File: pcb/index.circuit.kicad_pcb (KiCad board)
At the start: 2 copper layers, 102.2 x 63.8 mm, 36 parts, among them Q1 AO3401A, U1 ESP32_S3_WROOM_1_N16R8, U2 MAX98357AETE_T

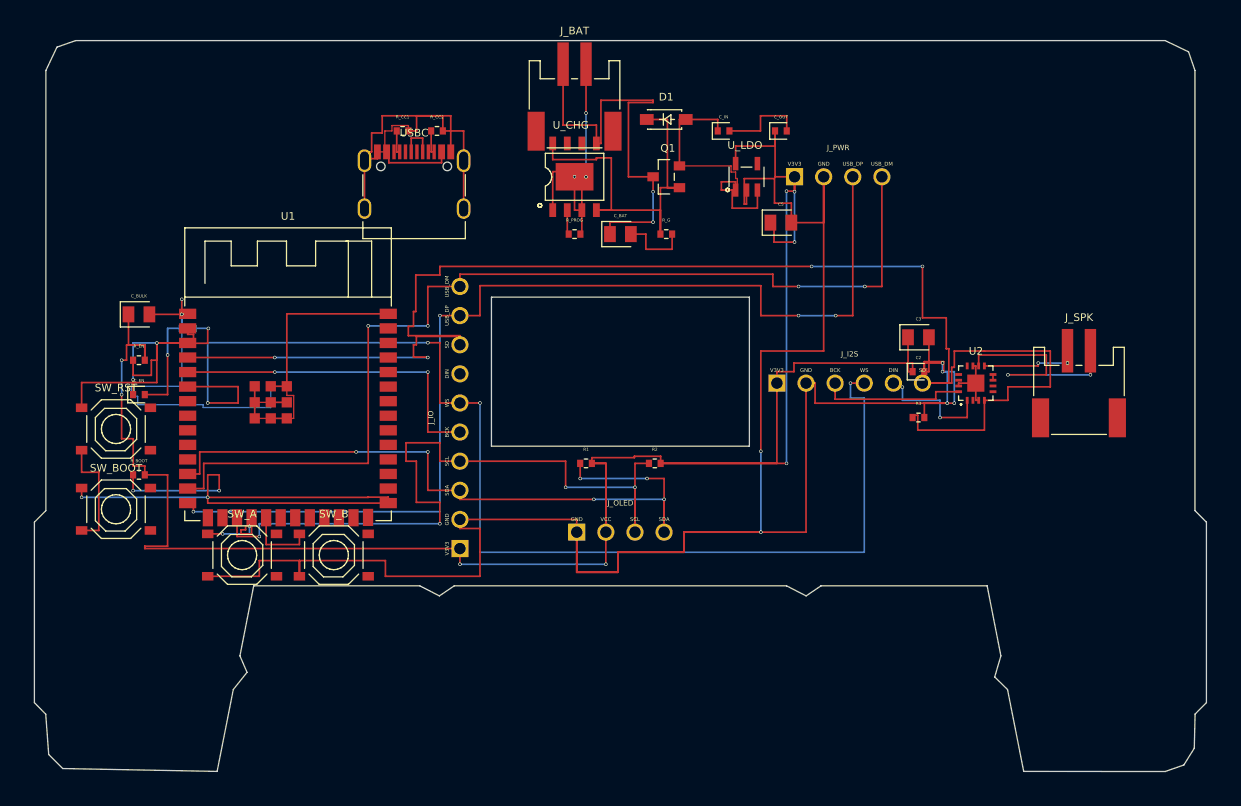
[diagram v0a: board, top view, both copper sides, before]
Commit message: pcb: fabbable cassette floorplan + headless IPC routing pipeline
Re-floorplan respecting ALL cassette cutouts (OLED window / 2 reel holes /
4 screw holes / bottom head-notch): spread the blocks across the board,
narrow the ESP32 column to fit beside the reel, and drop the now-redundant
breakout headers (J_IO/J_I2S/J_PWR) + reset/boot buttons (native-USB esptool
programming). All three placement gates pass: every part inside the outline,
0 courtyard overlaps, ~1 unrouted with the holes kept out. Routed via the IPC
pipeline (Freerouting -> kipy inject) with a GND pour; net fragments reconciled.

New place->route tooling (also in the global pcb-layout skill):
  route.sh, merge_nets.py, add_cutout_keepouts.py, drc_check.py,
  add_plane.py, apply_ses_ipc.py. Interior holes recovered from the CAD
  source of truth into lib/cassette_holes.json.

Co-Authored-By: Claude Opus 4.8 (1M context) <noreply@anthropic.com>
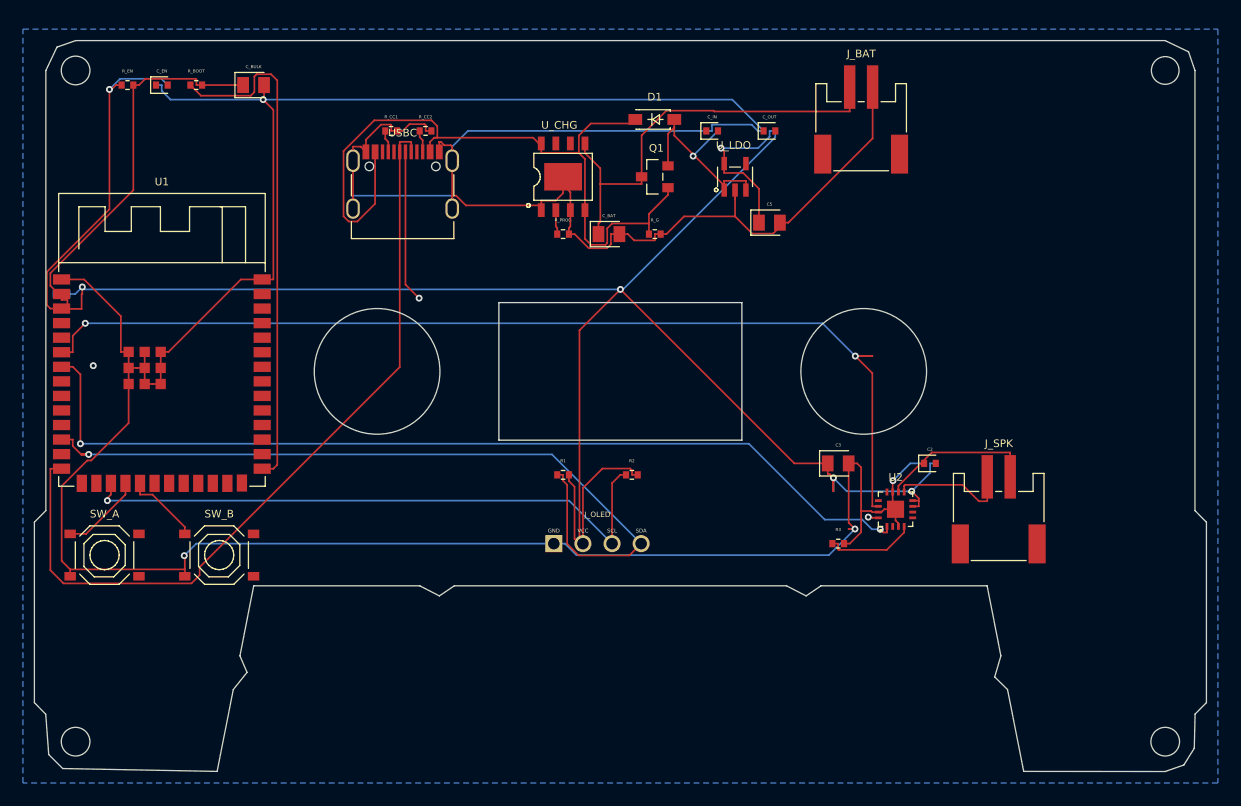
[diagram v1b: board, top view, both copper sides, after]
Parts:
- removed J_I2S: J_I2S, tscircuit:pin_header_pinrow6
- removed J_IO: J_IO, tscircuit:pin_header_pinrow10
- removed J_PWR: J_PWR, tscircuit:pin_header_pinrow4
- removed SW_BOOT, SW_RST: TS_1187A_B_A_B, tscircuit:TS_1187A_B_A_B
- moved R_BOOT 34.4 mm to (63.0, 72.0)
- moved C_EN 27.1 mm to (60.0, 72.0)
- moved J_BAT 25.1 mm to (121.0, 75.0)
- moved R_EN 24.0 mm to (57.0, 72.0)
- moved C_BULK 22.4 mm to (68.0, 72.0)
- moved C3 13.0 mm to (119.0, 105.0)
- moved J_SPK 13.0 mm to (133.0, 109.0)
- moved R3 13.0 mm to (119.0, 112.0)
- moved U2 13.0 mm to (124.0, 109.0)
- moved SW_A 12.0 mm to (55.0, 113.0)
- moved C1 11.4 mm to (51.2, 90.2)
- moved U1 11.4 mm to (60.0, 98.0)
- moved SW_B 10.0 mm to (65.0, 113.0)
- moved C2 8.06 mm to (127.0, 105.0)
- moved J_OLED 2.24 mm to (98.0, 112.0)
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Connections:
- J_OLED pad 3: .mcu .J_IO .SCL to .display .J_OLED .SCL -> SCL
- J_OLED pad 4: .mcu .J_IO .SDA to .display .J_OLED .SDA -> SDA
- R1 pad 2: J_OLED.VCC to net.V3V3 -> V3V3
- R2 pad 2: J_OLED.VCC to net.V3V3 -> V3V3
- R3 pad 1: J_I2S.SD to U2.SD_MODE -> SD
- U1 pad 12: U1.IO8 to J_IO.SDA -> SDA
- U1 pad 13: U1.IO19 to J_IO.USB_DM -> USB_DM
- U1 pad 14: U1.IO20 to J_IO.USB_DP -> USB_DP
- U1 pad 17: U1.IO9 to J_IO.SCL -> SCL
- U1 pad 4: U1.IO4 to J_IO.SD -> SD
- U1 pad 5: U1.IO5 to J_IO.BCK -> BCK
- U1 pad 6: U1.IO6 to J_IO.WS -> WS
- U1 pad 7: U1.IO7 to J_IO.DIN -> DIN
- U2 pad 1: J_I2S.DIN to U2.DIN -> DIN
- U2 pad 14: J_I2S.WS to U2.LRCLK -> WS
- U2 pad 16: J_I2S.BCK to U2.BCLK -> BCK
- U2 pad 4: J_I2S.SD to U2.SD_MODE -> SD
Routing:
- net WS: track 0.00 -> 92.5 mm, vias 0 -> 2
- net DIN: track 0.00 -> 82.1 mm, vias 0 -> 2
- net .mcu .J_IO .SD to .audio .J_I2S .SD: track 71.0 -> 0.00 mm, vias 2 -> 0
- net USB_DP: track 3.41 -> 70.5 mm
- net .mcu .J_IO .WS to .audio .J_I2S .WS: track 65.4 -> 0.00 mm, vias 2 -> 0
- net SDA: track 13.3 -> 71.3 mm, vias 2 -> 1
- net .power .J_PWR .USB_DP to .mcu .J_IO .USB_DP: track 51.6 -> 0.00 mm, vias 2 -> 0
- net .power .J_PWR .USB_DM to .mcu .J_IO .USB_DM: track 48.5 -> 0.00 mm, vias 2 -> 0
- net SCL: track 7.22 -> 54.0 mm, vias 0 -> 1
- net (no net): track 44.6 -> 0.00 mm
- net U1.IO20 to J_IO.USB_DP: track 41.6 -> 0.00 mm, vias 2 -> 0
- net U1.IO19 to J_IO.USB_DM: track 41.4 -> 0.00 mm, vias 2 -> 0
- net U1.IO6 to J_IO.WS: track 41.0 -> 0.00 mm, vias 2 -> 0
- net U1.IO9 to J_IO.SCL: track 36.8 -> 0.00 mm, vias 2 -> 0
- net J_I2S.SD to U2.SD_MODE: track 34.4 -> 0.00 mm
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- added copper zone on B.Cu, net GND
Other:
- outline, holes or cut-outs redrawn

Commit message: pcb: OLED as a placed part + keepout-respecting route
- Add the 0.96" SSD1306 OLED MODULE as a real placed part (custom footprint:
  4-pin header on solid board below the window + a 27x27mm body silkscreen
  outline over the window, on the BACK layer) so the drawing shows/reserves
  where it physically sits behind the tape window. Replaces the J_OLED header;
  buses route to OLED.SCL/SDA/VCC/GND.
- Re-route with cutout keepouts active and inject the keepout-respecting SES:
  geometric check confirms 0 track/via inside the reels or window (was crossing).
- outline-check: ALLOW_IN_CUTOUT (default "OLED") so a display intentionally
  behind a window isn't flagged.

Co-Authored-By: Claude Opus 4.8 (1M context) <noreply@anthropic.com>
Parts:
- removed J_OLED: J_OLED, tscircuit:pin_header_pinrow4
- added OLED: , tscircuit:chip, F.Cu at (100.0, 110.0)
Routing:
- net SDA: track 71.3 -> 4.70 mm, vias 1 -> 0
- net V3V3: track 205.3 -> 164.0 mm, vias 5 -> 4
- net USB_DM: track 13.3 -> 52.6 mm, vias 1 -> 2
- net USB_DP: track 70.5 -> 33.4 mm, vias 0 -> 1
- net GND: track 346.9 -> 334.3 mm, vias 4 -> 5
- net VBUS: track 66.4 -> 58.2 mm, vias 0 -> 2
- net U1.IO0 to R_BOOT.pin1: track 44.7 -> 36.6 mm
- net WS: track 92.5 -> 96.8 mm
- net VBAT: track 37.6 -> 40.9 mm
- net BCK: track 0.90 -> 3.78 mm
- net SCL: track 54.0 -> 51.6 mm
- net DIN: track 82.1 -> 79.7 mm
- net SD: track 7.94 -> 10.0 mm, vias 0 -> 1
- net U1.EN to R_EN.pin1: track 29.4 -> 30.4 mm
- net U2.OUTP to J_SPK.pin1: track 10.5 -> 11.1 mm

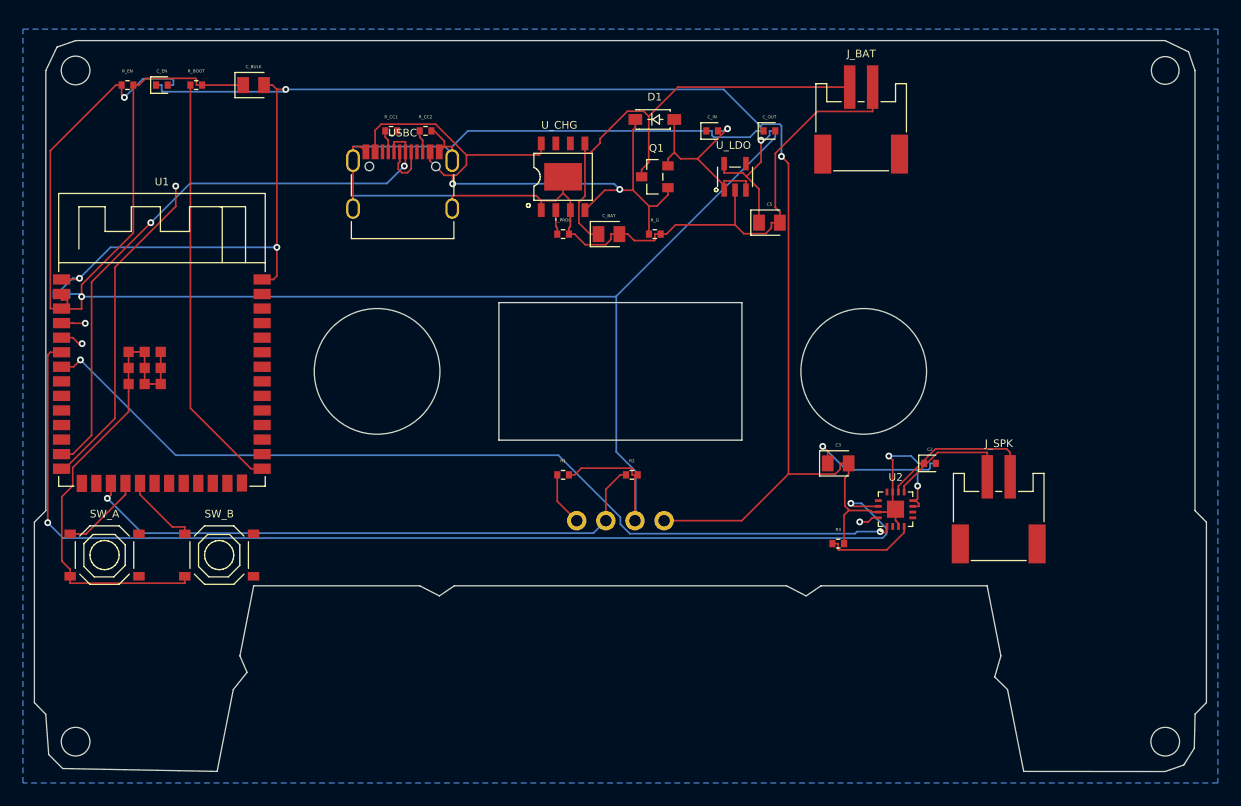
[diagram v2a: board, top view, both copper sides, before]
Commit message: pcb: fix window keepout + JLC DRC rules -> DRC 216->23 cosmetic
- add_cutout_keepouts: poly regex missed the window (newline before pts close
  paren) so it was never kept out; one trace crossed it. Fixed -> 7 interiors
  detected (window + 2 reels + 4 screws), re-routed, segment check = 0 copper
  inside any hole.
- apply_fab_rules.py: set .kicad_pro DRC to JLCPCB mins (clearance 0.127,
  copper-edge 0.2, min-text 0.25) + ignore non-fab cosmetic checks
  (lib_footprint, silk, back-text). Cosmetic DRC 216 -> 23; real tail =
  3 shorts + 13 unconnected.
- apply_ses_ipc: drop the endpoint-snap experiment (added crossings/shorts).

Co-Authored-By: Claude Opus 4.8 (1M context) <noreply@anthropic.com>
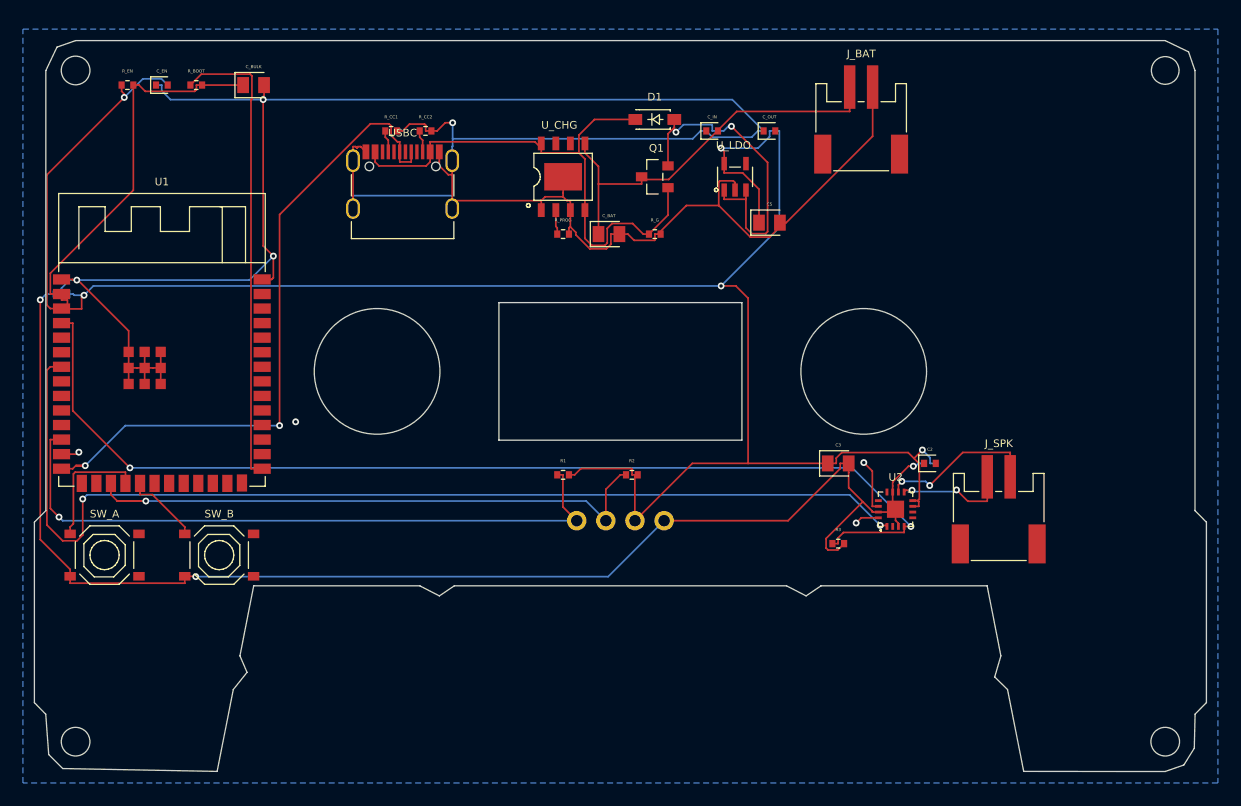
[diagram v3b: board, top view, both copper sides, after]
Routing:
- net WS: track 96.8 -> 4.65 mm, vias 2 -> 1
- net SD: track 10.0 -> 94.0 mm, vias 1 -> 2
- net SDA: track 4.70 -> 58.3 mm, vias 0 -> 1
- net USB_DM: track 52.6 -> 1.58 mm
- net USB_DP: track 33.4 -> 60.8 mm, vias 1 -> 2
- net V3V3: track 164.0 -> 188.7 mm
- net GND: track 334.3 -> 358.9 mm, vias 5 -> 7
- net DIN: track 79.7 -> 93.4 mm
- net VSYS: track 18.0 -> 29.2 mm, vias 1 -> 2
- net VBUS: track 58.2 -> 49.0 mm, vias 2 -> 0
- net SCL: track 51.6 -> 60.1 mm
- net VBAT: track 40.9 -> 35.5 mm
- net U1.IO0 to R_BOOT.pin1: track 36.6 -> 41.1 mm
- net U1.IO10 to SW_A.A: track 7.22 -> 10.9 mm
- net U1.EN to R_EN.pin1: track 30.4 -> 28.2 mm
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
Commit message: pcb+cad: U1 re-floorplan (fix edge spills) + 3D fit-check + JLCPCB fab tooling
- pcb: move MCU off the left board edge (-40 -> -38) and clean re-route;
  obstacle-aware surgical short fixes -> 0 shorts / 0 crossings / 0 edge-over-cut
- drc_check: promote copper AT/OVER the board cut (edge clearance <= 0.05mm) to a
  real blocking class; it was hidden inside the cosmetic bucket
- cad/import_pcb.py + render_fit.py: bring the routed board into the printed-cassette
  assembly as STL -- bare KiCad board for layer registration, populated tscircuit
  board (component bodies from the CDN models) for connector clearance; `make fit`
- gen_bom_cpl.py + `make fab`: JLCPCB gerber+drill zip and assembly BOM/CPL
- render/render_assembly.py: use the real pcb.stl in place of the flat stand-in

Co-Authored-By: Claude Opus 4.8 (1M context) <noreply@anthropic.com>
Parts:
- moved C1 2.00 mm to (53.2, 90.2)
- moved C_BULK 2.00 mm to (70.0, 72.0)
- moved C_EN 2.00 mm to (62.0, 72.0)
- moved R_BOOT 2.00 mm to (65.0, 72.0)
- moved R_EN 2.00 mm to (59.0, 72.0)
- moved SW_A 2.00 mm to (57.0, 113.0)
- moved SW_B 2.00 mm to (67.0, 113.0)
- moved U1 2.00 mm to (62.0, 98.0)
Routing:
- net DIN: track 93.4 -> 0.00 mm, vias 2 -> 0
- net BCK: track 2.12 -> 81.4 mm, vias 1 -> 2
- net WS: track 4.65 -> 77.3 mm, vias 1 -> 2
- net USB_DM: track 1.58 -> 67.5 mm
- net VBUS: track 49.0 -> 67.4 mm
- net SCL: track 60.1 -> 49.8 mm
- net GND: track 358.9 -> 350.0 mm, vias 7 -> 9
- net V3V3: track 188.7 -> 197.4 mm, vias 4 -> 5
- net VSYS: track 29.2 -> 20.8 mm, vias 2 -> 1
- net SDA: track 58.3 -> 51.6 mm
- net SD: track 94.0 -> 87.5 mm
- net U1.IO0 to R_BOOT.pin1: track 41.1 -> 36.6 mm
- net USB_DP: track 60.8 -> 63.2 mm, vias 2 -> 0
- net U1.IO10 to SW_A.A: track 10.9 -> 8.90 mm
- net VBAT: track 35.5 -> 37.2 mm
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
